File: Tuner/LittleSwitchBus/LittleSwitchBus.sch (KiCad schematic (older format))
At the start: 99 parts, among them J1 Conn_Coaxial, J10 Conn_Coaxial, J11 Conn_02x05_Odd_Even, J13 Conn_01x01, J14 Conn_01x01, J15 Conn_01x01, J16 Conn_01x01, J2 Conn_Coaxial, J3 Conn_Coaxial, J4 Conn_Coaxial, J5 Conn_Coaxial, J6 Conn_Coaxial, J7 Conn_Coaxial, J8 Conn_Coaxial, J9 Conn_Coaxial, U1 MCP23008, U2 ULN2803A

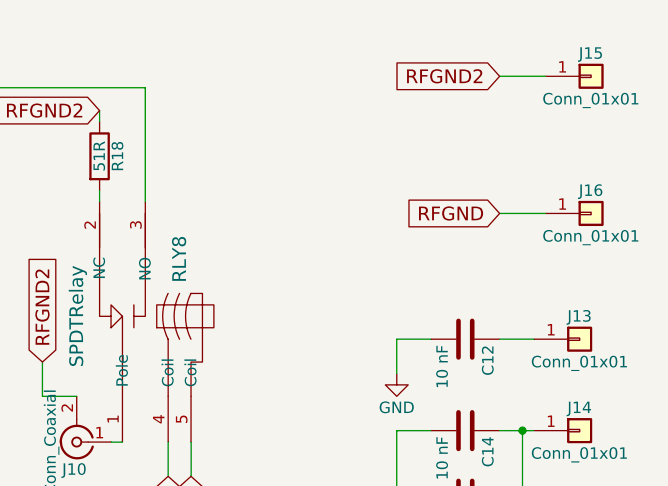
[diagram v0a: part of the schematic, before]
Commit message: Added extra capacitors between relay power and ground posts
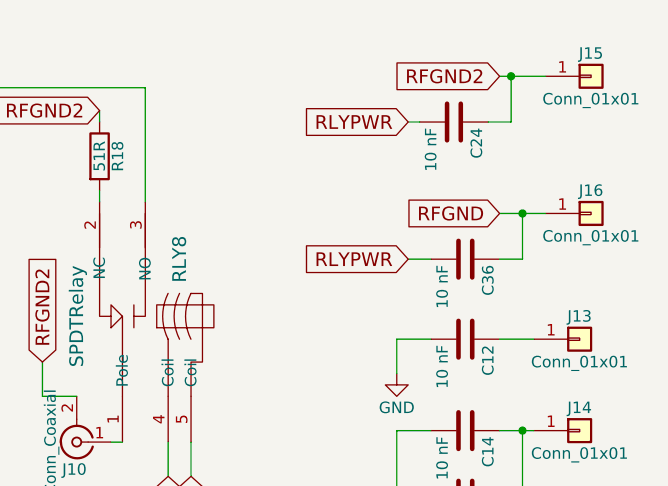
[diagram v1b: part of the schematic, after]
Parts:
- added C24, C36: 10 nF, Capacitors_THT:C_Disc_D5.0mm_W2.5mm_P2.50mm, symbol C
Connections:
- net RFGND: now also C36.1
- net RFGND2: now also C24.1
- net RLYPWR: now also C24.2, C36.2
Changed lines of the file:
@@
 RLY8
 $Comp
-L +5V #PWR01
+L +5V #PWR11
 U 1 1 5B1A0287
 P 3150 5750
-F 0 "#PWR01" H 3150 5600 50  0001 C CNN
+F 0 "#PWR11" H 3150 5600 50  0001 C CNN
 F 1 "+5V" H 3150 5890 50  0000 C CNN
 F 2 "" H 3150 5750 50  0001 C CNN
@@
 $EndComp
 $Comp
-L GND #PWR02
+L GND #PWR3
 U 1 1 5B1AA0F6
 P 900 4500
-F 0 "#PWR02" H 900 4250 50  0001 C CNN
+F 0 "#PWR3" H 900 4250 50  0001 C CNN
 F 1 "GND" H 900 4350 50  0000 C CNN
 F 2 "" H 900 4500 50  0001 C CNN
@@
 $EndComp
 $Comp
-L +5V #PWR03
+L +5V #PWR2
 U 1 1 5B1AABE9
 P 900 3750
-F 0 "#PWR03" H 900 3600 50  0001 C CNN
+F 0 "#PWR2" H 900 3600 50  0001 C CNN
 F 1 "+5V" H 900 3890 50  0000 C CNN
 F 2 "" H 900 3750 50  0001 C CNN
@@
 $EndComp
 $Comp
-L +5V #PWR04
+L +5V #PWR8
 U 1 1 5B1ABA5A
 P 2150 4450
-F 0 "#PWR04" H 2150 4300 50  0001 C CNN
+F 0 "#PWR8" H 2150 4300 50  0001 C CNN
 F 1 "+5V" H 2150 4590 50  0000 C CNN
 F 2 "" H 2150 4450 50  0001 C CNN
@@
 $EndComp
 $Comp
-L +5V #PWR05
+L +5V #PWR16
 U 1 1 5B1ABFC6
 P 8800 4600
-F 0 "#PWR05" H 8800 4450 50  0001 C CNN
+F 0 "#PWR16" H 8800 4450 50  0001 C CNN
 F 1 "+5V" H 8800 4740 50  0000 C CNN
 F 2 "" H 8800 4600 50  0001 C CNN
@@
 $EndComp
 $Comp
-L GND #PWR06
+L GND #PWR17
 U 1 1 5B1AC04C
 P 8800 5150
-F 0 "#PWR06" H 8800 4900 50  0001 C CNN
+F 0 "#PWR17" H 8800 4900 50  0001 C CNN
 F 1 "GND" H 8800 5000 50  0000 C CNN
 F 2 "" H 8800 5150 50  0001 C CNN
@@
 $EndComp
 $Comp
-L GND #PWR07
+L GND #PWR14
 U 1 1 5B9A4AE1
 P 4850 6650
-F 0 "#PWR07" H 4850 6400 50  0001 C CNN
+F 0 "#PWR14" H 4850 6400 50  0001 C CNN
 F 1 "GND" H 4850 6500 50  0000 C CNN
 F 2 "" H 4850 6650 50  0001 C CNN
@@
 $EndComp
 $Comp
-L GND #PWR08
+L GND #PWR13
 U 1 1 5B9ACA36
 P 3550 6100
-F 0 "#PWR08" H 3550 5850 50  0001 C CNN
+F 0 "#PWR13" H 3550 5850 50  0001 C CNN
 F 1 "GND" H 3550 5950 50  0000 C CNN
 F 2 "" H 3550 6100 50  0001 C CNN
@@
 $EndComp
 $Comp
-L GND #PWR09
+L GND #PWR18
 U 1 1 5B982525
 P 10250 2050
-F 0 "#PWR09" H 10250 1800 50  0001 C CNN
+F 0 "#PWR18" H 10250 1800 50  0001 C CNN
 F 1 "GND" H 10250 1900 50  0000 C CNN
 F 2 "" H 10250 2050 50  0001 C CNN
@@
 $EndComp
 $Comp
-L GND #PWR010
+L GND #PWR7
 U 1 1 5BA4D8F3
 P 1800 5850
-F 0 "#PWR010" H 1800 5600 50  0001 C CNN
+F 0 "#PWR7" H 1800 5600 50  0001 C CNN
 F 1 "GND" H 1800 5700 50  0000 C CNN
 F 2 "" H 1800 5850 50  0001 C CNN
@@
 $EndComp
 $Comp
-L +5V #PWR011
+L +5V #PWR6
 U 1 1 5BA4E663
 P 1200 5700
-F 0 "#PWR011" H 1200 5550 50  0001 C CNN
+F 0 "#PWR6" H 1200 5550 50  0001 C CNN
 F 1 "+5V" H 1200 5840 50  0000 C CNN
 F 2 "" H 1200 5700 50  0001 C CNN
@@
 $EndComp
 $Comp
-L GND #PWR012
+L GND #PWR1
 U 1 1 5BA4FB25
 P 750 5900
-F 0 "#PWR012" H 750 5650 50  0001 C CNN
+F 0 "#PWR1" H 750 5650 50  0001 C CNN
 F 1 "GND" H 750 5750 50  0000 C CNN
 F 2 "" H 750 5900 50  0001 C CNN
@@
 $EndComp
 $Comp
-L GND #PWR013
+L GND #PWR5
 U 1 1 5BA5005D
 P 1100 5300
-F 0 "#PWR013" H 1100 5050 50  0001 C CNN
+F 0 "#PWR5" H 1100 5050 50  0001 C CNN
 F 1 "GND" H 1100 5150 50  0000 C CNN
 F 2 "" H 1100 5300 50  0001 C CNN
@@
 EXTPWR
 $Comp
-L +5V #PWR014
+L +5V #PWR4
 U 1 1 5BAE4DBC
 P 1000 4850
-F 0 "#PWR014" H 1000 4700 50  0001 C CNN
+F 0 "#PWR4" H 1000 4700 50  0001 C CNN
 F 1 "+5V" H 1000 4990 50  0000 C CNN
 F 2 "" H 1000 4850 50  0001 C CNN
@@
 $EndComp
 $Comp
-L GND #PWR015
+L GND #PWR15
 U 1 1 5BAEE216
 P 5050 7250
-F 0 "#PWR015" H 5050 7000 50  0001 C CNN
+F 0 "#PWR15" H 5050 7000 50  0001 C CNN
 F 1 "GND" H 5050 7100 50  0000 C CNN
 F 2 "" H 5050 7250 50  0001 C CNN
@@
 $EndComp
 $Comp
-L +5V #PWR016
+L +5V #PWR9
 U 1 1 5C7585CE
 P 2250 4000
-F 0 "#PWR016" H 2250 3850 50  0001 C CNN
+F 0 "#PWR9" H 2250 3850 50  0001 C CNN
 F 1 "+5V" H 2250 4140 50  0000 C CNN
 F 2 "" H 2250 4000 50  0001 C CNN
@@
 $EndComp
 $Comp
-L +5V #PWR017
+L +5V #PWR10
 U 1 1 5C7589BF
 P 2400 4000
-F 0 "#PWR017" H 2400 3850 50  0001 C CNN
+F 0 "#PWR10" H 2400 3850 50  0001 C CNN
 F 1 "+5V" H 2400 4140 50  0000 C CNN
 F 2 "" H 2400 4000 50  0001 C CNN
@@
 $EndComp
 $Comp
-L GND #PWR018
+L GND #PWR12
 U 1 1 5C758F92
 P 3300 4250
-F 0 "#PWR018" H 3300 4000 50  0001 C CNN
+F 0 "#PWR12" H 3300 4000 50  0001 C CNN
 F 1 "GND" H 3300 4100 50  0000 C CNN
 F 2 "" H 3300 4250 50  0001 C CNN
@@
 Wire Wire Line
 	10700 750  10900 750
+Text GLabel 10300 950  0    60   Input ~ 0
+RLYPWR
+$Comp
+L C C24
+U 1 1 5DDBBD8B
+P 10500 950
+F 0 "C24" H 10525 1050 50  0000 L CNN
+F 1 "10 nF" H 10525 850 50  0000 L CNN
+F 2 "Capacitors_THT:C_Disc_D5.0mm_W2.5mm_P2.50mm" H 10538 800 50  0001 C CNN
+F 3 "" H 10500 950 50  0001 C CNN
+	1    10500 950
+	0    1    1    0
+$EndComp
+Wire Wire Line
+	10350 950  10300 950
+Wire Wire Line
+	10750 750  10750 950
+Wire Wire Line
+	10750 950  10650 950
+Connection ~ 10750 750
+Text GLabel 10300 1550 0    60   Input ~ 0
+RLYPWR
+$Comp
+L C C36
+U 1 1 5DDBC527
+P 10550 1550
+F 0 "C36" H 10575 1650 50  0000 L CNN
+F 1 "10 nF" H 10575 1450 50  0000 L CNN
+F 2 "Capacitors_THT:C_Disc_D5.0mm_W2.5mm_P2.50mm" H 10588 1400 50  0001 C CNN
+F 3 "" H 10550 1550 50  0001 C CNN
+	1    10550 1550
+	0    1    1    0
+$EndComp
+Wire Wire Line
+	10400 1550 10300 1550
+Wire Wire Line
+	10800 1350 10800 1550
+Wire Wire Line
+	10800 1550 10700 1550
+Connection ~ 10800 1350
 $EndSCHEMATC

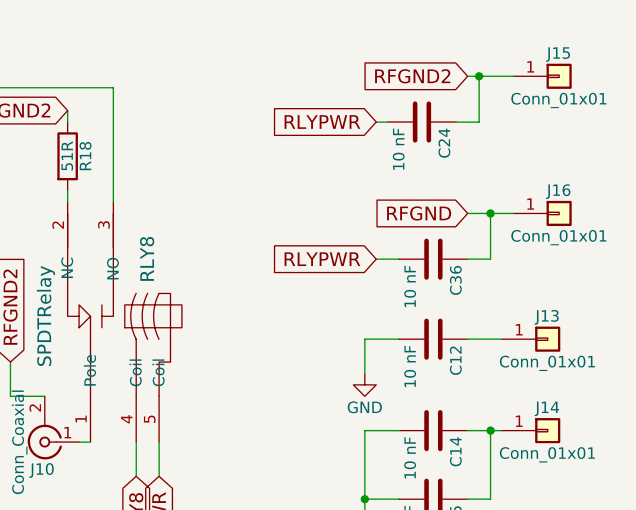
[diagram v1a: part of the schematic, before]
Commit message: Changed some of the capacitors to NC becaue they might cause problems in some situations
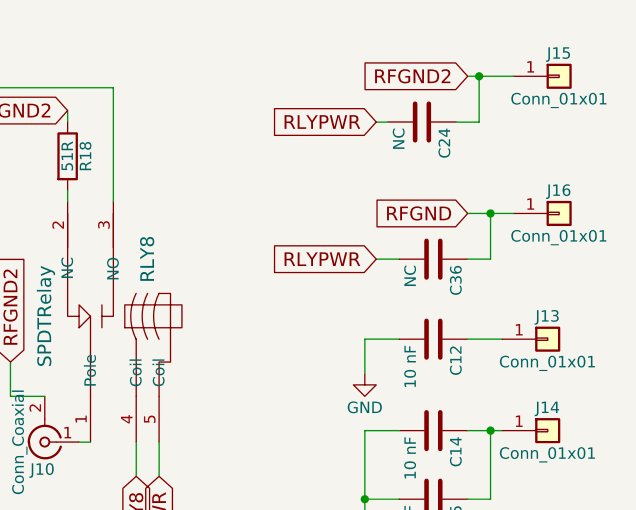
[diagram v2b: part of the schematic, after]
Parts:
- C24, C36: value 10 nF -> NC
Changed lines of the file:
@@
 P 10500 950
 F 0 "C24" H 10525 1050 50  0000 L CNN
-F 1 "10 nF" H 10525 850 50  0000 L CNN
+F 1 "NC" H 10525 850 50  0000 L CNN
 F 2 "Capacitors_THT:C_Disc_D5.0mm_W2.5mm_P2.50mm" H 10538 800 50  0001 C CNN
 F 3 "" H 10500 950 50  0001 C CNN
@@
 P 10550 1550
 F 0 "C36" H 10575 1650 50  0000 L CNN
-F 1 "10 nF" H 10575 1450 50  0000 L CNN
+F 1 "NC" H 10575 1450 50  0000 L CNN
 F 2 "Capacitors_THT:C_Disc_D5.0mm_W2.5mm_P2.50mm" H 10588 1400 50  0001 C CNN
 F 3 "" H 10550 1550 50  0001 C CNN
